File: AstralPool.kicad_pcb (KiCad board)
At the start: 2 copper layers, 80 x 75 mm, 25 parts, among them J1 RJ12, J2 RJ12, J3 Header, Q1 2N3904, U1 LM2678T-5.0/NOPB

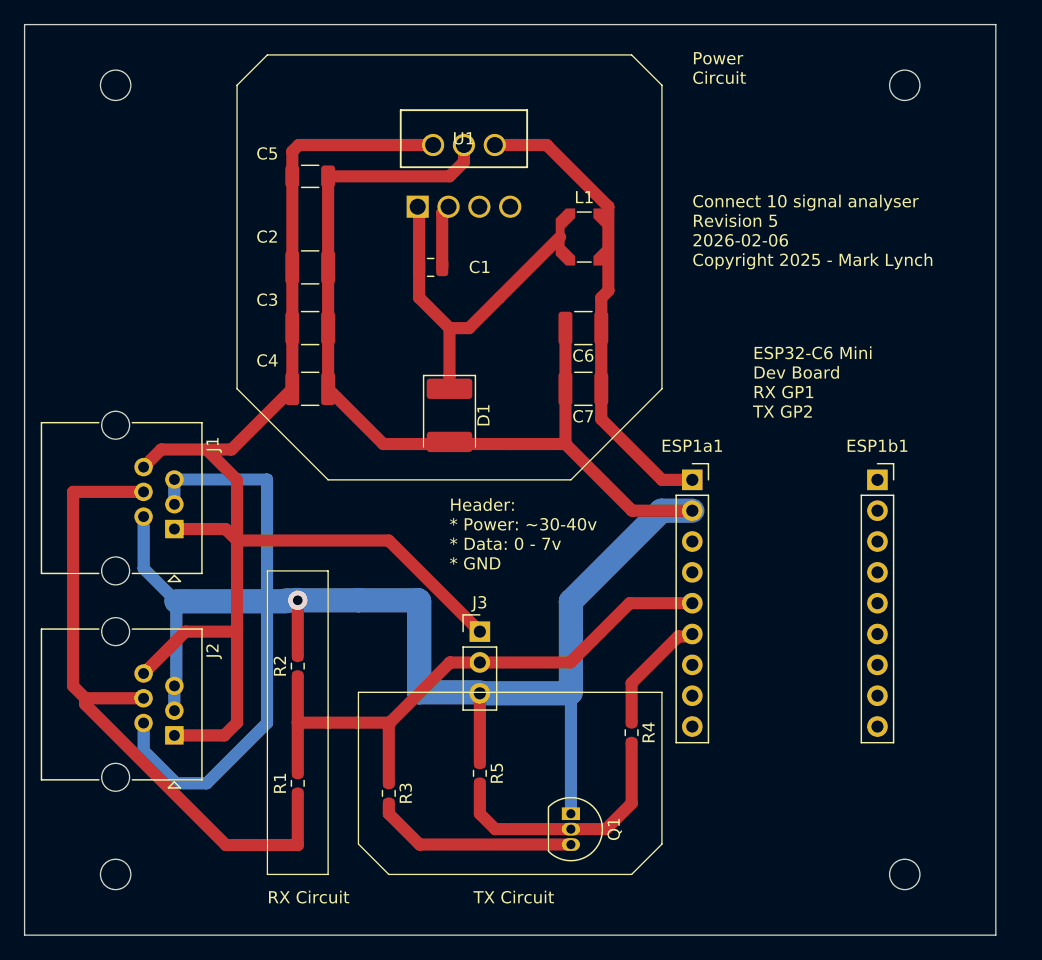
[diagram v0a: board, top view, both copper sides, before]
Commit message: ### Fixed - Fixed all the DRC rule violations and all but one of the ERC issues - Make the component imports be relative paths
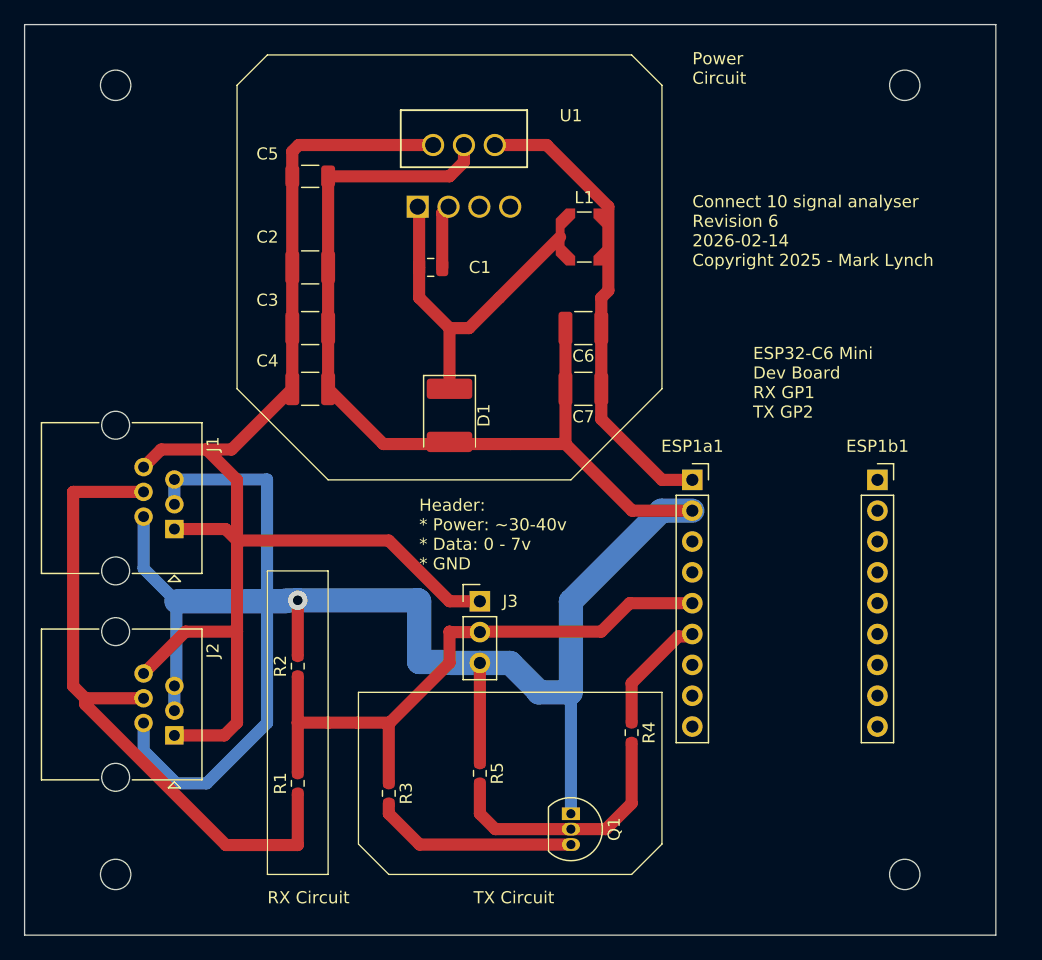
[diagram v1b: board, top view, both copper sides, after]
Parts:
- moved J3 2.50 mm to (92.5, 70.0)
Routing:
- net Net-(ESP1a1-Pin_5): track 49.6 -> 51.2 mm
- net GND (from connector): track 217.8 -> 218.9 mm
- net +24V (from connector): track 113.2 -> 112.2 mm
